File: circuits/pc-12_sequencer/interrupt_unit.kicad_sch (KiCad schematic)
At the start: 5 parts, among them U10 74HC74, U9 4011

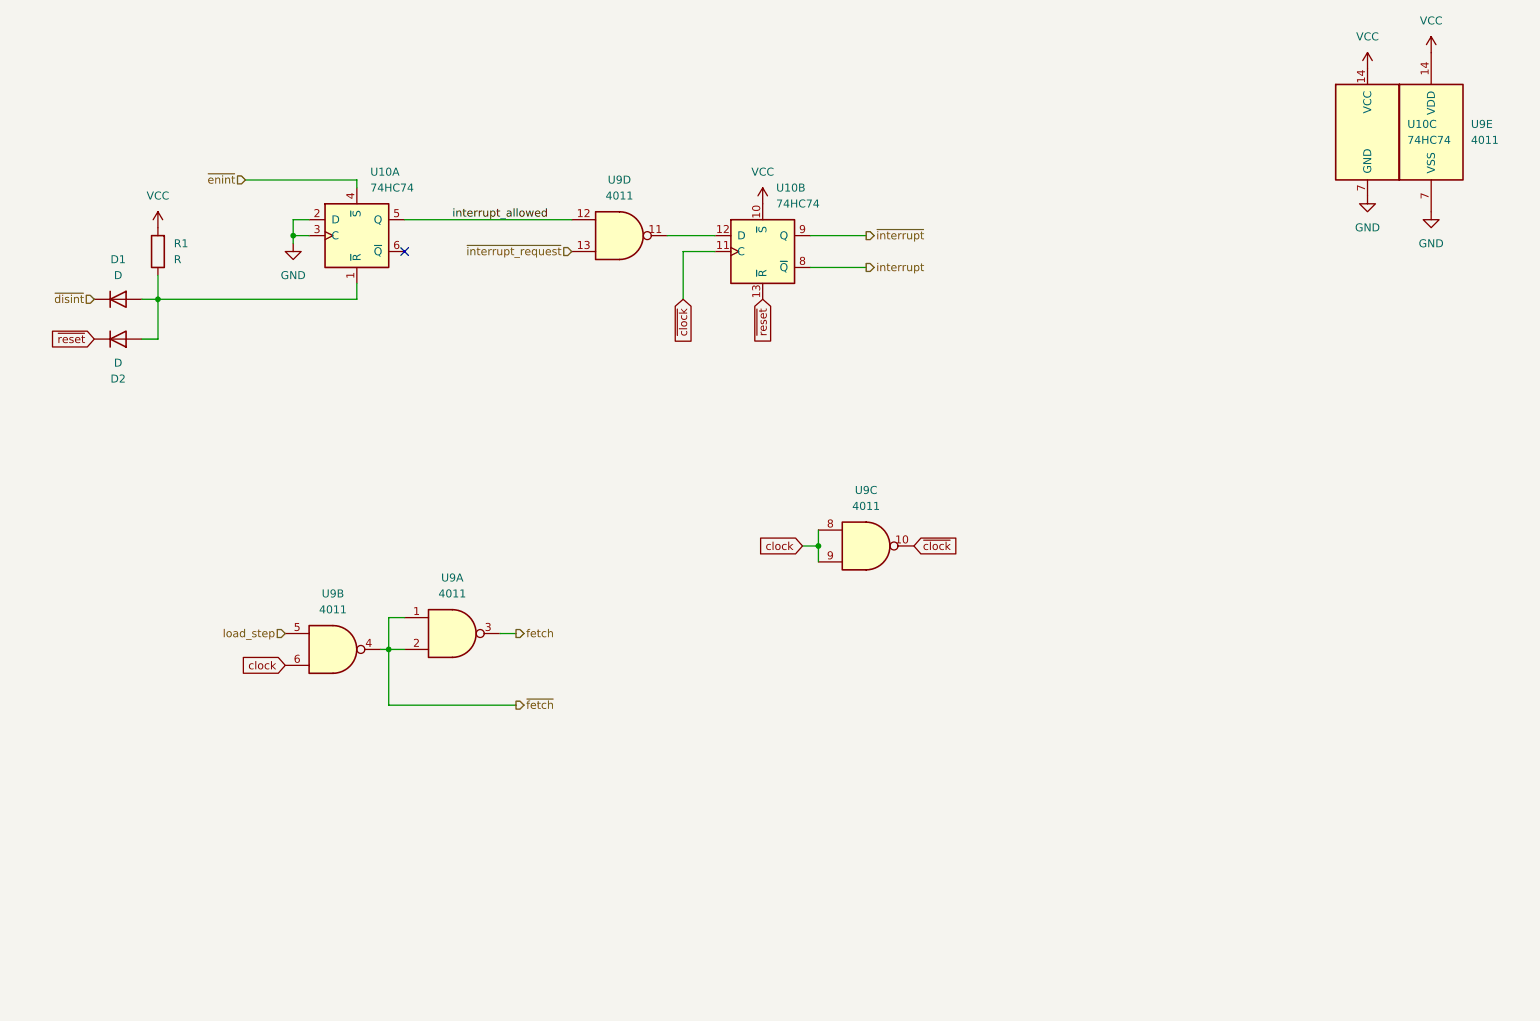
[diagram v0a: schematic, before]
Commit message: reworking sequencer PCB
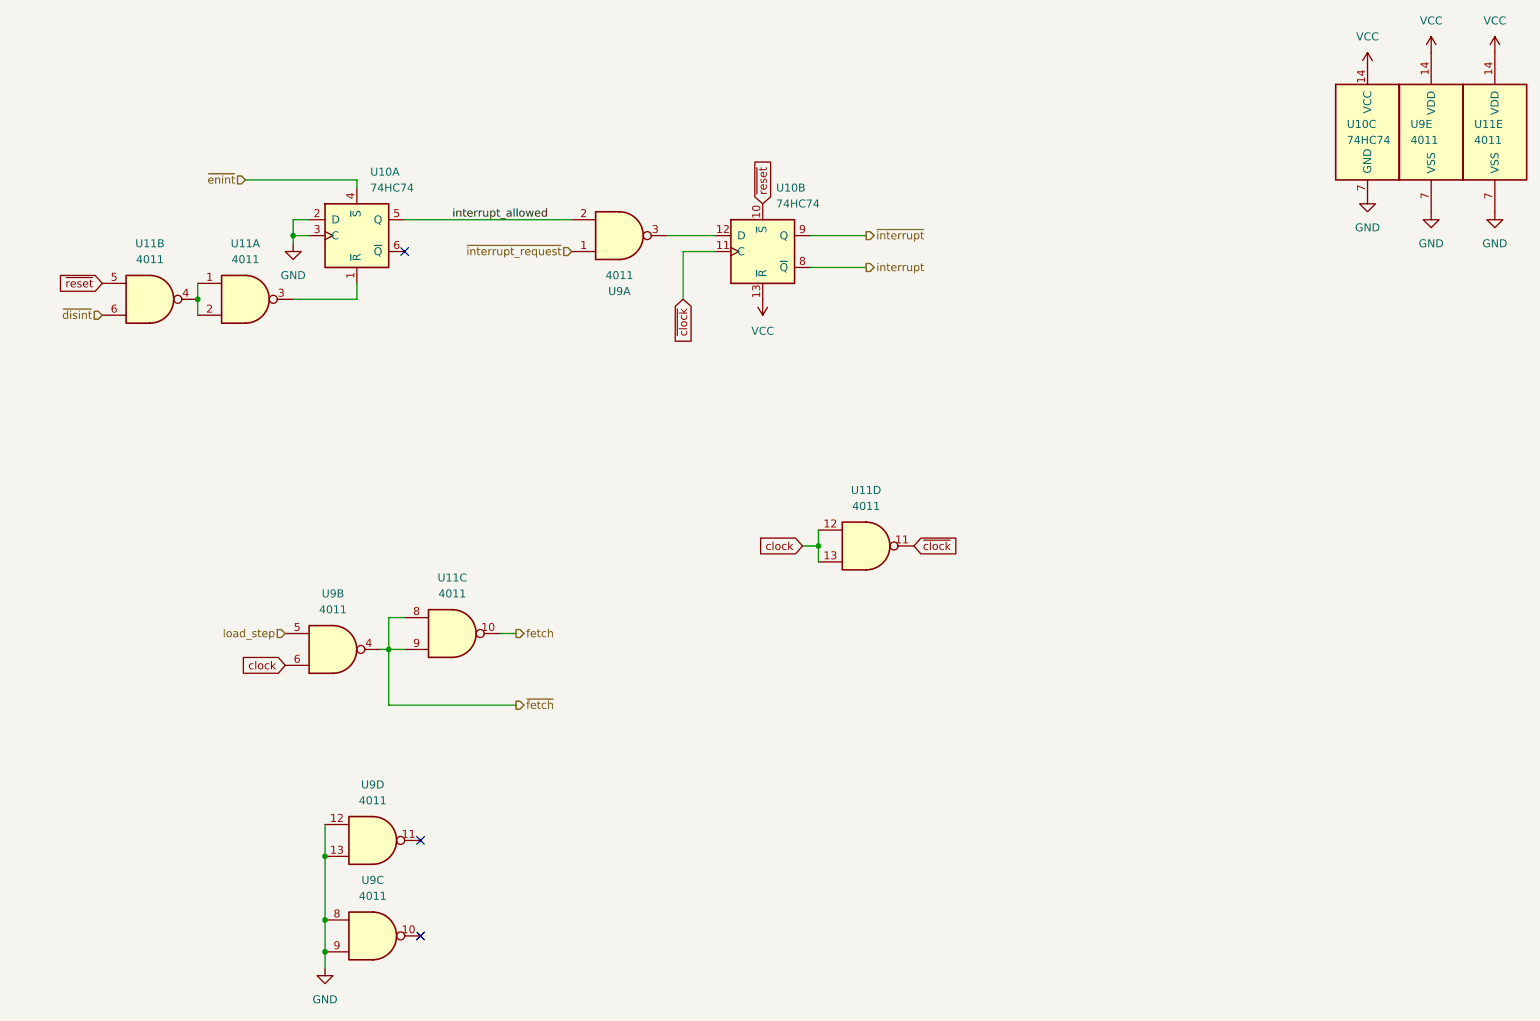
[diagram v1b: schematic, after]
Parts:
- removed D1, D2: D, Diode_THT:D_DO-35_SOD27_P2.54mm_Vertical_KathodeUp, symbol Device:D
- removed R1: R, Resistor_SMD:R_0603_1608Metric, symbol Device:R
- added U11: 4011, Package_DIP:DIP-14_W7.62mm, symbol 4xxx:4011
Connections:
- net GND: now also U9.12, U9.13, U9.8, U9.9, U11.7 (VSS)
- net VCC: now also U10.13 (~{R}), U11.14 (VDD); no longer U10.10 (~{S})
- net clock: now also U11.12, U11.13; no longer U9.8, U9.9
- net fetch: now also U11.10; no longer U9.3
- net interrupt_allowed: now also U9.2; no longer U9.12
- net ~{clock}: now also U11.11; no longer U9.10
- net ~{disint}: now also U11.6
- net ~{fetch}: now also U11.8, U11.9; no longer U9.1, U9.2
- net ~{interrupt_request}: now also U9.1; no longer U9.13
- net ~{reset}: now also U10.10 (~{S}), U11.5; no longer U10.13 (~{R})
- net at U9.11: no longer U10.12 (D)
- net at U10.1 (~{R}): now also U11.3
- new net: U10.12 (D), U9.3
- new net: U11.1, U11.2, U11.4
- no-connect marks 1 -> 3
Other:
- moved on the sheet: U9A, U9C, U9D

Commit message: finalize rev. a of pc-12
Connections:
- net GND: now also U9.5, U9.6; no longer U9.12, U9.13, U9.8, U9.9
- net clock: now also U9.8; no longer U9.6
- net load_step: now also U9.9; no longer U9.5
- net ~{fetch}: now also U9.10; no longer U9.4
- net ~{interrupt_request}: now also U9.12, U9.13; no longer U9.1
- net at U9.11: now also U9.1
- no-connect marks 3 -> 2
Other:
- moved on the sheet: U9B, U9C, U9D
